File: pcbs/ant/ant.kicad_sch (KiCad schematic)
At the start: 17 parts, among them SW1 SW_PUSH, SW10 SW_PUSH, SW11 SW_PUSH, SW12 SW_PUSH, SW13 SW_PUSH, SW14 SW_PUSH, SW2 SW_PUSH, SW3 SW_PUSH, SW4 SW_PUSH, SW5 SW_PUSH, SW6 SW_PUSH, SW7 SW_PUSH, SW8 SW_PUSH, SW9 SW_PUSH, U1 ProMicro

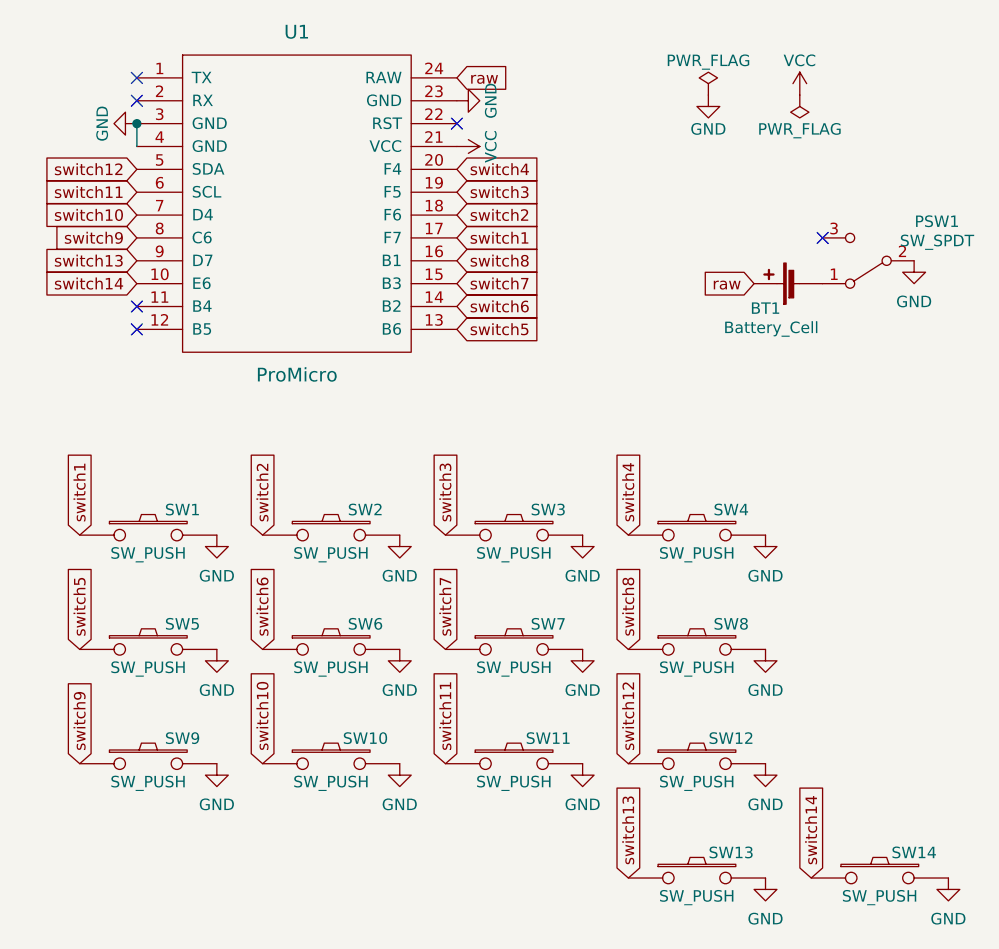
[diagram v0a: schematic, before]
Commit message: Dropped a key from the Ant.
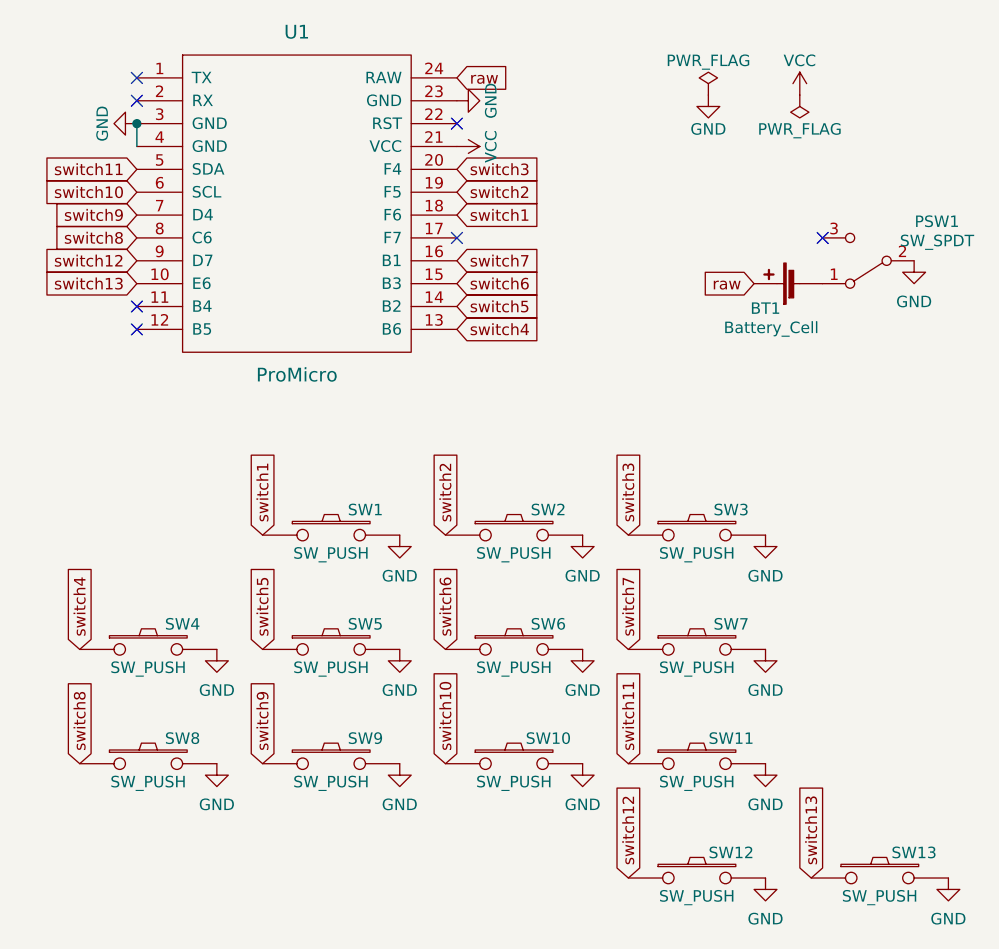
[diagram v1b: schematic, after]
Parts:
- removed SW1: SW_PUSH, bugs:Choc_reversible, symbol knott:SW_PUSH-kbd
- renumbered SW2 to SW1, SW11 to SW10, SW12 to SW11, SW13 to SW12, SW14 to SW13, SW3 to SW2, SW4 to SW3, SW5 to SW4, SW6 to SW5, SW7 to SW6, SW8 to SW7, SW9 to SW8, SW10 to SW9
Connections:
- net switch14 is gone; now on net switch13: SW13.1, U1.10 (E6)
- net switch1: now also SW1.1, U1.18 (F6); no longer U1.17 (F7)
- net switch10: now also SW10.1, U1.6 (SCL); no longer SW9.1, U1.7 (D4)
- net switch11: now also SW11.1, U1.5 (SDA); no longer SW10.1, U1.6 (SCL)
- net switch12: now also SW12.1, U1.9 (D7); no longer SW11.1, U1.5 (SDA)
- net switch13: no longer SW12.1, U1.9 (D7)
- net switch2: now also SW2.1, U1.19 (F5); no longer SW1.1, U1.18 (F6)
- net switch3: now also SW3.1, U1.20 (F4); no longer SW2.1, U1.19 (F5)
- net switch4: now also SW4.1, U1.13 (B6); no longer SW3.1, U1.20 (F4)
- net switch5: now also SW5.1, U1.14 (B2); no longer SW4.1, U1.13 (B6)
- net switch6: now also SW6.1, U1.15 (B3); no longer SW5.1, U1.14 (B2)
- net switch7: now also SW7.1, U1.16 (B1); no longer SW6.1, U1.15 (B3)
- net switch8: now also SW8.1, U1.8 (C6); no longer SW7.1, U1.16 (B1)
- net switch9: now also SW9.1, U1.7 (D4); no longer SW8.1, U1.8 (C6)
- no-connect marks 6 -> 7
